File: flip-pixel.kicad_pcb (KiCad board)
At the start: 2 copper layers, 177 parts, among them Q1 DMN62D0U-7, Q10 STS8DN6LF6AG, Q11 DMN62D0U-7, Q12 DMN62D0U-7, Q13 STS8DN6LF6AG, Q14 DMN62D0U-7, Q15 DMN62D0U-7, Q16 STS8DN6LF6AG, Q17 DMN62D0U-7, Q18 DMN62D0U-7, Q19 STS8DN6LF6AG, Q2 DMN62D0U-7, Q20 DMN62D0U-7, Q21 DMN62D0U-7, Q22 STS8DN6LF6AG, Q23 DMN62D0U-7, Q24 DMN62D0U-7, Q25 STS8DN6LF6AG, Q26 DMN62D0U-7, Q27 DMN62D0U-7, Q28 STS8DN6LF6AG, Q29 DMN62D0U-7, Q3 DMN62D0U-7, Q30 DMN62D0U-7, Q31 STS8DN6LF6AG, Q4 STS8DN6LF6AG, Q5 DMN62D0U-7, Q6 DMN62D0U-7, Q7 STS8DN6LF6AG, Q8 DMN62D0U-7, Q9 DMN62D0U-7, U1 LM2665M6

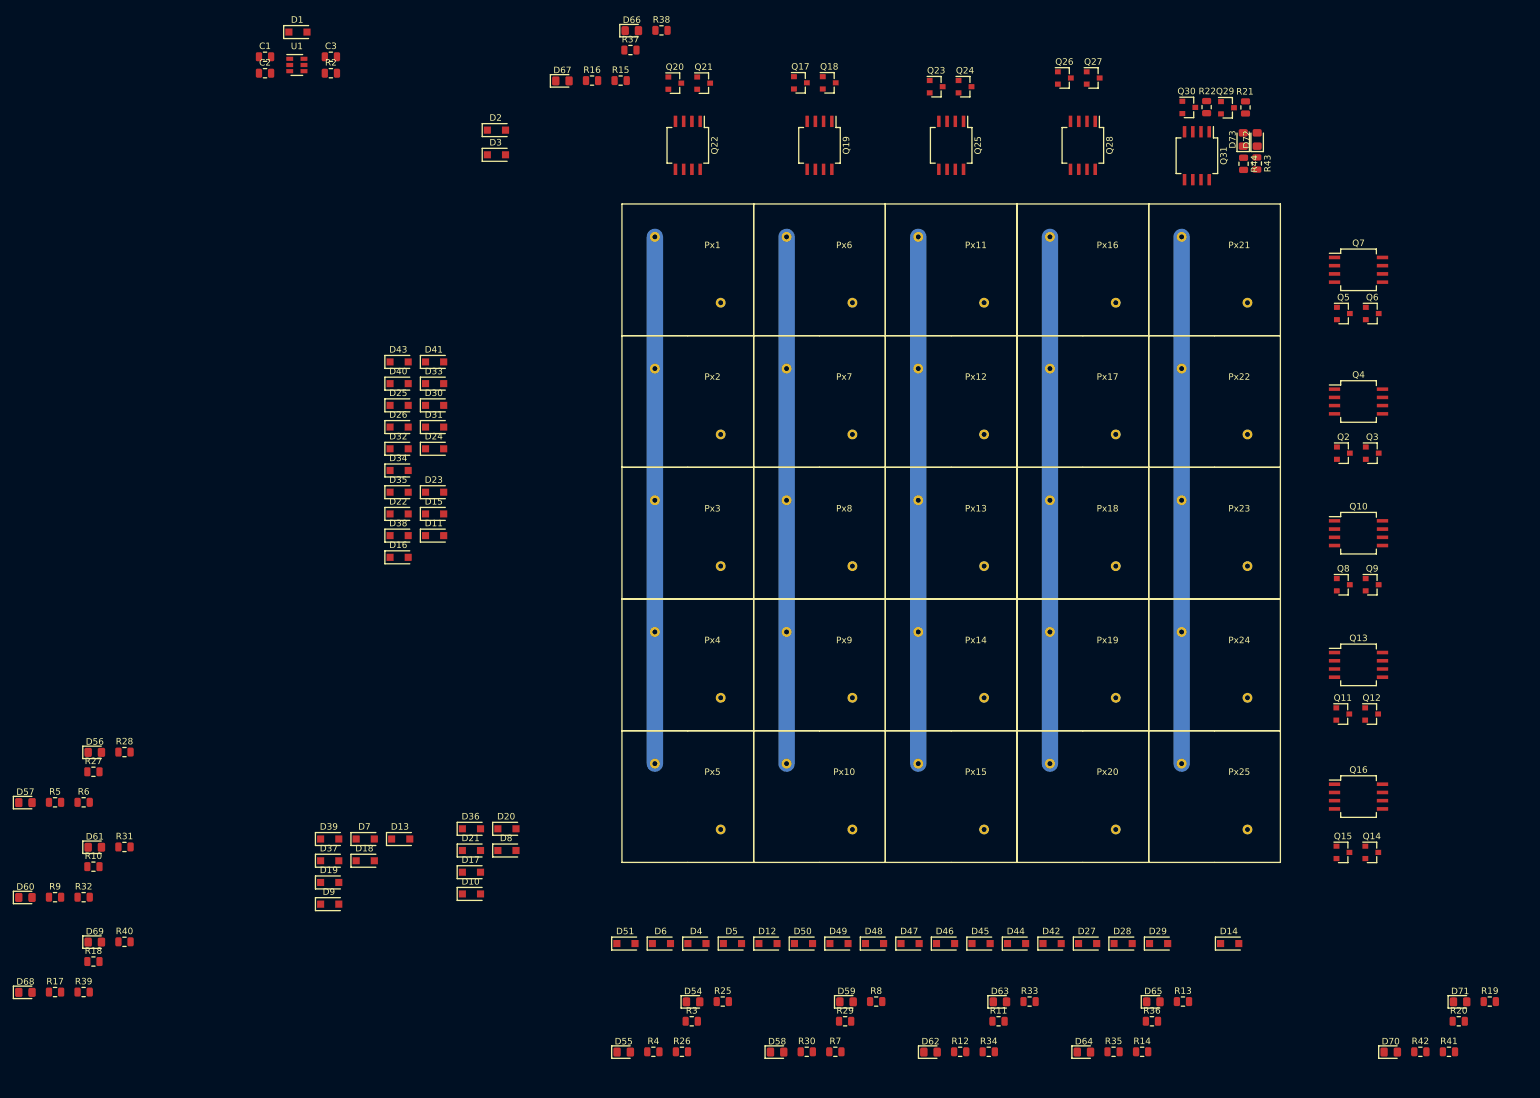
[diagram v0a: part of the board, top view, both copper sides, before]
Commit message: Pixel Matrix and started Driving Circuits
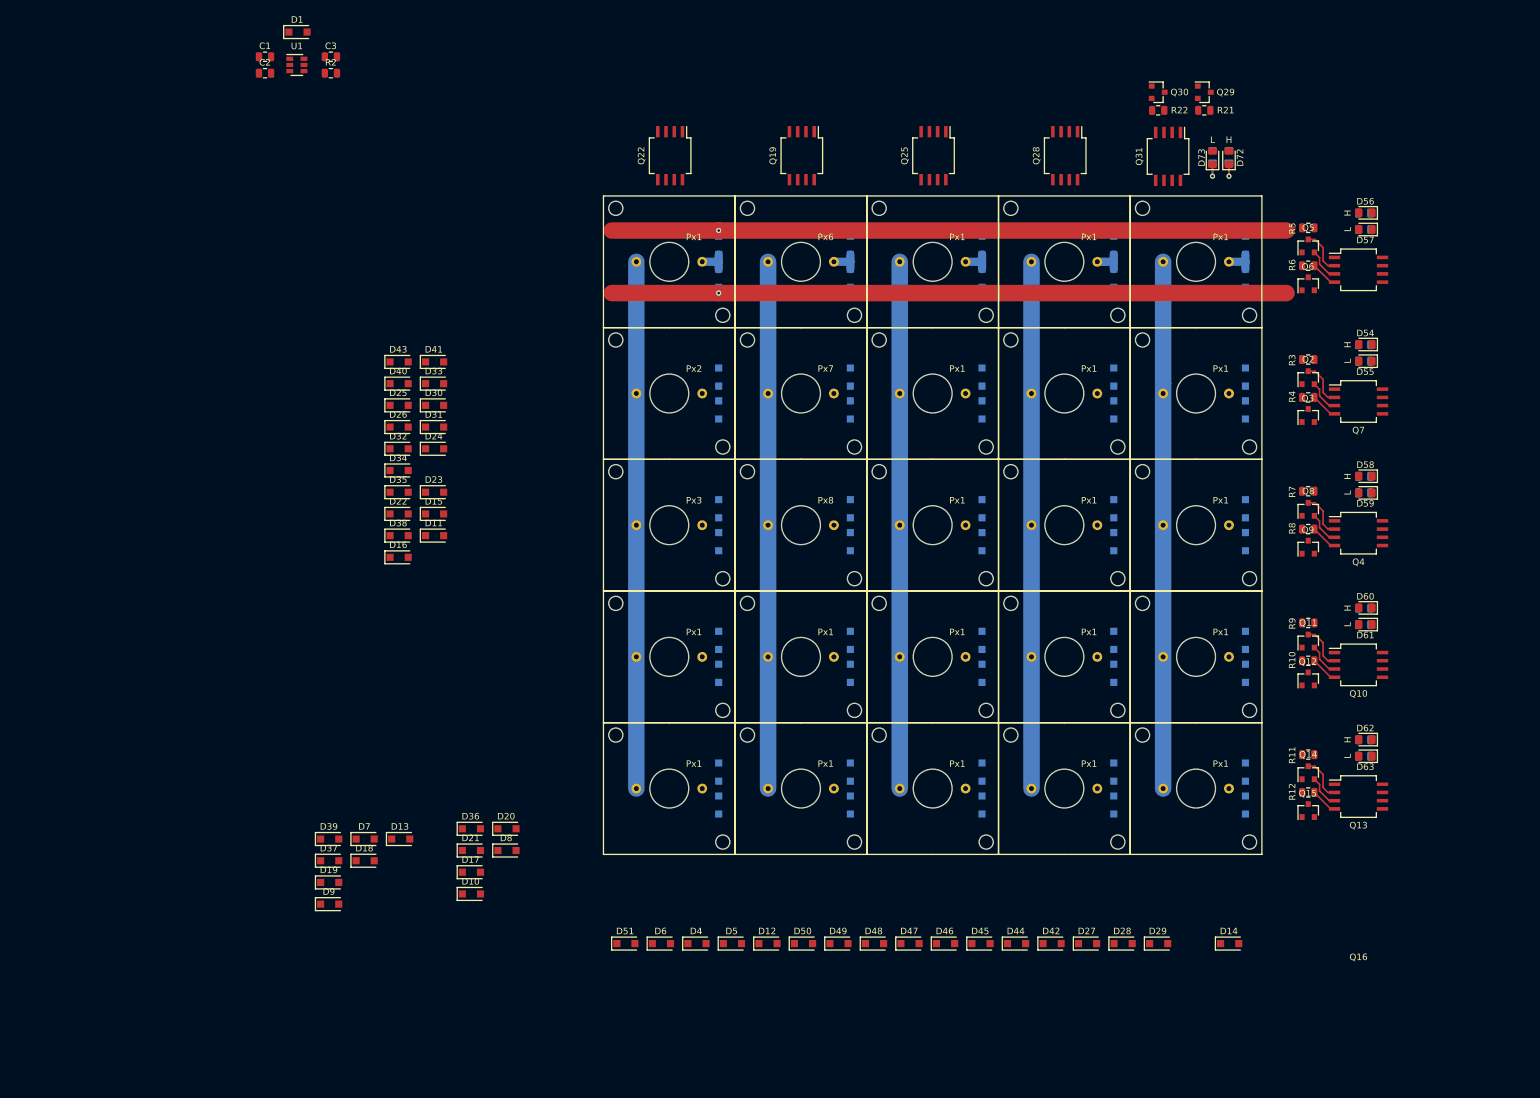
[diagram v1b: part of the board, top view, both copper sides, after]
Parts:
- removed the D2 at (141.0, 31.8)
- removed the D3 at (141.0, 35.6)
- removed D64, D65, D66, D67, D68, D69, D70, D71: LED_Green, LED_SMD:LED_0805_2012Metric_Pad1.15x1.40mm_HandSolder
- removed the Px1 at (170.5, 53.3)
- removed Px10, Px11, Px12, Px13, Px14, Px15, Px16, Px17, Px18, Px19, Px20, Px21, Px22, Px23, Px24, Px25, Px4, Px5, Px9: FlipPixel, Custom-Footprints:Flip-Pixel
- removed Q17, Q18, Q20, Q21, Q23, Q24, Q26, Q27: DMN62D0U-7, Package_TO_SOT_SMD:SOT-23
- removed R13, R14, R15, R16, R17, R18, R19, R20, R35, R36, R37, R38, R39, R40, R41, R42: R, Resistor_SMD:R_0805_2012Metric
- added D2: Diode, Diode_SMD:D_SOD-123F, B.Cu at (256.5, 130.8)
- added D2: Diode, Diode_SMD:D_SOD-123F, B.Cu at (236.2, 49.5)
- added D2: Diode, Diode_SMD:D_SOD-123F, B.Cu at (215.9, 130.8)
- added D2: Diode, Diode_SMD:D_SOD-123F, B.Cu at (215.9, 110.5)
- added D2: Diode, Diode_SMD:D_SOD-123F, B.Cu at (215.9, 90.2)
- added D2: Diode, Diode_SMD:D_SOD-123F, B.Cu at (215.9, 69.8)
- added D2: Diode, Diode_SMD:D_SOD-123F, B.Cu at (215.9, 49.5)
- added D2: Diode, Diode_SMD:D_SOD-123F, B.Cu at (195.6, 130.8)
- added D2: Diode, Diode_SMD:D_SOD-123F, B.Cu at (195.6, 110.5)
- added D2: Diode, Diode_SMD:D_SOD-123F, B.Cu at (195.6, 90.2)
- added D2: Diode, Diode_SMD:D_SOD-123F, B.Cu at (195.6, 69.8)
- added D2: Diode, Diode_SMD:D_SOD-123F, B.Cu at (256.5, 110.5)
- added D2: Diode, Diode_SMD:D_SOD-123F, B.Cu at (195.6, 49.5)
- added D2: Diode, Diode_SMD:D_SOD-123F, B.Cu at (175.3, 130.8)
- added D2: Diode, Diode_SMD:D_SOD-123F, B.Cu at (175.3, 110.5)
- added D2: Diode, Diode_SMD:D_SOD-123F, B.Cu at (175.3, 90.2)
- added D2: Diode, Diode_SMD:D_SOD-123F, B.Cu at (175.3, 69.8)
- added D2: Diode, Diode_SMD:D_SOD-123F, B.Cu at (175.3, 49.5)
- added D2: Diode, Diode_SMD:D_SOD-123F, B.Cu at (256.5, 90.2)
- added D2: Diode, Diode_SMD:D_SOD-123F, B.Cu at (256.5, 69.8)
- added D2: Diode, Diode_SMD:D_SOD-123F, B.Cu at (256.5, 49.5)
- added D2: Diode, Diode_SMD:D_SOD-123F, B.Cu at (236.2, 130.8)
- added D2: Diode, Diode_SMD:D_SOD-123F, B.Cu at (236.2, 110.5)
- added D2: Diode, Diode_SMD:D_SOD-123F, B.Cu at (236.2, 90.2)
- added D2: Diode, Diode_SMD:D_SOD-123F, B.Cu at (236.2, 69.8)
- added D3: Diode, Diode_SMD:D_SOD-123F, B.Cu at (256.5, 135.9)
- added D3: Diode, Diode_SMD:D_SOD-123F, B.Cu at (236.2, 54.6)
- added D3: Diode, Diode_SMD:D_SOD-123F, B.Cu at (215.9, 135.9)
- added D3: Diode, Diode_SMD:D_SOD-123F, B.Cu at (215.9, 115.6)
- added D3: Diode, Diode_SMD:D_SOD-123F, B.Cu at (215.9, 95.2)
- added D3: Diode, Diode_SMD:D_SOD-123F, B.Cu at (215.9, 74.9)
- added D3: Diode, Diode_SMD:D_SOD-123F, B.Cu at (215.9, 54.6)
- added D3: Diode, Diode_SMD:D_SOD-123F, B.Cu at (195.6, 135.9)
- added D3: Diode, Diode_SMD:D_SOD-123F, B.Cu at (195.6, 115.6)
- added D3: Diode, Diode_SMD:D_SOD-123F, B.Cu at (195.6, 95.2)
- added D3: Diode, Diode_SMD:D_SOD-123F, B.Cu at (195.6, 74.9)
- added D3: Diode, Diode_SMD:D_SOD-123F, B.Cu at (256.5, 115.6)
- added D3: Diode, Diode_SMD:D_SOD-123F, B.Cu at (195.6, 54.6)
- added D3: Diode, Diode_SMD:D_SOD-123F, B.Cu at (175.3, 135.9)
- added D3: Diode, Diode_SMD:D_SOD-123F, B.Cu at (175.3, 115.6)
- added D3: Diode, Diode_SMD:D_SOD-123F, B.Cu at (175.3, 95.2)
- added D3: Diode, Diode_SMD:D_SOD-123F, B.Cu at (175.3, 74.9)
- added D3: Diode, Diode_SMD:D_SOD-123F, B.Cu at (175.3, 54.6)
- added D3: Diode, Diode_SMD:D_SOD-123F, B.Cu at (256.5, 95.2)
- added D3: Diode, Diode_SMD:D_SOD-123F, B.Cu at (256.5, 74.9)
- added D3: Diode, Diode_SMD:D_SOD-123F, B.Cu at (256.5, 54.6)
- added D3: Diode, Diode_SMD:D_SOD-123F, B.Cu at (236.2, 135.9)
- added D3: Diode, Diode_SMD:D_SOD-123F, B.Cu at (236.2, 115.6)
- added D3: Diode, Diode_SMD:D_SOD-123F, B.Cu at (236.2, 95.2)
- added D3: Diode, Diode_SMD:D_SOD-123F, B.Cu at (236.2, 74.9)
- added Px1: FlipPixel, Custom-Footprints:Flip-Pixel, F.Cu at (248.9, 133.3)
- added Px1: FlipPixel, Custom-Footprints:Flip-Pixel, F.Cu at (228.6, 52.1)
- added Px1: FlipPixel, Custom-Footprints:Flip-Pixel, F.Cu at (208.3, 133.3)
- added Px1: FlipPixel, Custom-Footprints:Flip-Pixel, F.Cu at (208.3, 113.0)
- added Px1: FlipPixel, Custom-Footprints:Flip-Pixel, F.Cu at (208.3, 92.7)
- added Px1: FlipPixel, Custom-Footprints:Flip-Pixel, F.Cu at (208.3, 72.4)
- added Px1: FlipPixel, Custom-Footprints:Flip-Pixel, F.Cu at (208.3, 52.1)
- added Px1: FlipPixel, Custom-Footprints:Flip-Pixel, F.Cu at (188.0, 133.3)
- added Px1: FlipPixel, Custom-Footprints:Flip-Pixel, F.Cu at (188.0, 113.0)
- added Px1: FlipPixel, Custom-Footprints:Flip-Pixel, F.Cu at (167.6, 133.3)
- added Px1: FlipPixel, Custom-Footprints:Flip-Pixel, F.Cu at (167.6, 113.0)
- added Px1: FlipPixel, Custom-Footprints:Flip-Pixel, F.Cu at (248.9, 113.0)
- added Px1: FlipPixel, Custom-Footprints:Flip-Pixel, F.Cu at (167.6, 52.1)
- added Px1: FlipPixel, Custom-Footprints:Flip-Pixel, F.Cu at (248.9, 92.7)
- added Px1: FlipPixel, Custom-Footprints:Flip-Pixel, F.Cu at (248.9, 72.4)
- added Px1: FlipPixel, Custom-Footprints:Flip-Pixel, F.Cu at (248.9, 52.1)
- added Px1: FlipPixel, Custom-Footprints:Flip-Pixel, F.Cu at (228.6, 133.3)
- added Px1: FlipPixel, Custom-Footprints:Flip-Pixel, F.Cu at (228.6, 113.0)
- added Px1: FlipPixel, Custom-Footprints:Flip-Pixel, F.Cu at (228.6, 92.7)
- added Px1: FlipPixel, Custom-Footprints:Flip-Pixel, F.Cu at (228.6, 72.4)
- R25, R26, R27, R28, R29, R30, R31, R32, R33, R34, R43, R44: moved to B.Cu
- moved D57 224.9 mm to (275.0, 47.1), turned to 180 degrees
- moved R27 214.2 mm to (274.9, 44.5), turned to 180 degrees
- moved D56 213.0 mm to (275.0, 44.5), turned to 180 degrees
- moved R5 212.7 mm to (266.2, 46.8)
- moved D60 211.5 mm to (275.0, 105.5), turned to 180 degrees
- moved R28 207.6 mm to (274.9, 47.1), turned to 180 degrees
- moved R6 206.3 mm to (266.2, 52.7)
- moved R32 202.0 mm to (274.9, 108.0), turned to 180 degrees
- moved D61 199.0 mm to (275.0, 108.0), turned to 180 degrees
- moved R9 197.9 mm to (266.2, 107.8)
- moved R31 194.8 mm to (274.9, 105.5), turned to 180 degrees
- moved R10 190.1 mm to (266.2, 113.6)
- moved D55 156.4 mm to (275.0, 67.4), turned to 180 degrees
- moved R26 149.8 mm to (274.9, 67.4), turned to 180 degrees
- moved D54 145.1 mm to (275.0, 64.8), turned to 180 degrees
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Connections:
- Px2 pad 1: Net-(D4-Pad1) -> Net-(D2-Pad1)
- Px3 pad 1: Net-(D6-Pad1) -> Net-(D2-Pad1)
- Px6 pad 1: Net-(D12-Pad1) -> Net-(D2-Pad1)
- Px6 pad 2: /PixelMatrix/Col_2 -> /PixelMatrix/Col_1
- Px7 pad 1: Net-(D14-Pad1) -> Net-(D2-Pad1)
- Px7 pad 2: /PixelMatrix/Col_2 -> /PixelMatrix/Col_1
- Px8 pad 1: Net-(D16-Pad1) -> Net-(D2-Pad1)
- Px8 pad 2: /PixelMatrix/Col_2 -> /PixelMatrix/Col_1
- Q19 pad 1: /PixelMatrix/Col_2 -> /PixelMatrix/Col_5
- Q19 pad 2: /Column2/Gate_H -> /Column5/Gate_H
- Q19 pad 4: /Column2/Gate_L -> /Column5/Gate_L
- Q19 pad 5: /PixelMatrix/Col_2 -> /PixelMatrix/Col_5
- Q19 pad 6: /PixelMatrix/Col_2 -> /PixelMatrix/Col_5
- Q22 pad 1: /PixelMatrix/Col_1 -> /PixelMatrix/Col_5
- Q22 pad 2: /Column1/Gate_H -> /Column5/Gate_H
- Q22 pad 4: /Column1/Gate_L -> /Column5/Gate_L
- Q22 pad 5: /PixelMatrix/Col_1 -> /PixelMatrix/Col_5
- Q22 pad 6: /PixelMatrix/Col_1 -> /PixelMatrix/Col_5
- Q25 pad 1: /PixelMatrix/Col_3 -> /PixelMatrix/Col_5
- Q25 pad 2: /Column3/Gate_H -> /Column5/Gate_H
- Q25 pad 4: /Column3/Gate_L -> /Column5/Gate_L
- Q25 pad 5: /PixelMatrix/Col_3 -> /PixelMatrix/Col_5
- Q25 pad 6: /PixelMatrix/Col_3 -> /PixelMatrix/Col_5
- Q28 pad 1: /PixelMatrix/Col_4 -> /PixelMatrix/Col_5
- Q28 pad 2: /Column4/Gate_H -> /Column5/Gate_H
- Q28 pad 4: /Column4/Gate_L -> /Column5/Gate_L
- Q28 pad 5: /PixelMatrix/Col_4 -> /PixelMatrix/Col_5
- Q28 pad 6: /PixelMatrix/Col_4 -> /PixelMatrix/Col_5
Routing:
- net /PixelMatrix/Col_1: track 81.3 -> 406.4 mm
- net /Row1/Low: track 0.00 -> 105.0 mm, vias 0 -> 1
- net /Row1/High: track 0.00 -> 105.0 mm, vias 0 -> 1
- net /PixelMatrix/Col_5: track 81.3 -> 0.00 mm
- net /PixelMatrix/Col_4: track 81.3 -> 0.00 mm
- net /PixelMatrix/Col_3: track 81.3 -> 0.00 mm
- net /PixelMatrix/Col_2: track 81.3 -> 0.00 mm
- net GND: track 0.00 -> 25.4 mm
- net Net-(D2-Pad1): track 0.00 -> 24.1 mm
- net /Row5/Gate_H: track 0.00 -> 6.93 mm
- net /Row3/Gate_H: track 0.00 -> 6.93 mm
- net /Row4/Gate_H: track 0.00 -> 6.93 mm
- net /Row2/Gate_H: track 0.00 -> 6.93 mm
- net /Row1/Gate_H: track 0.00 -> 6.93 mm
- net /Row5/Gate_L: track 0.00 -> 4.17 mm
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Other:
- board text added: "H"
- board text added: "L"

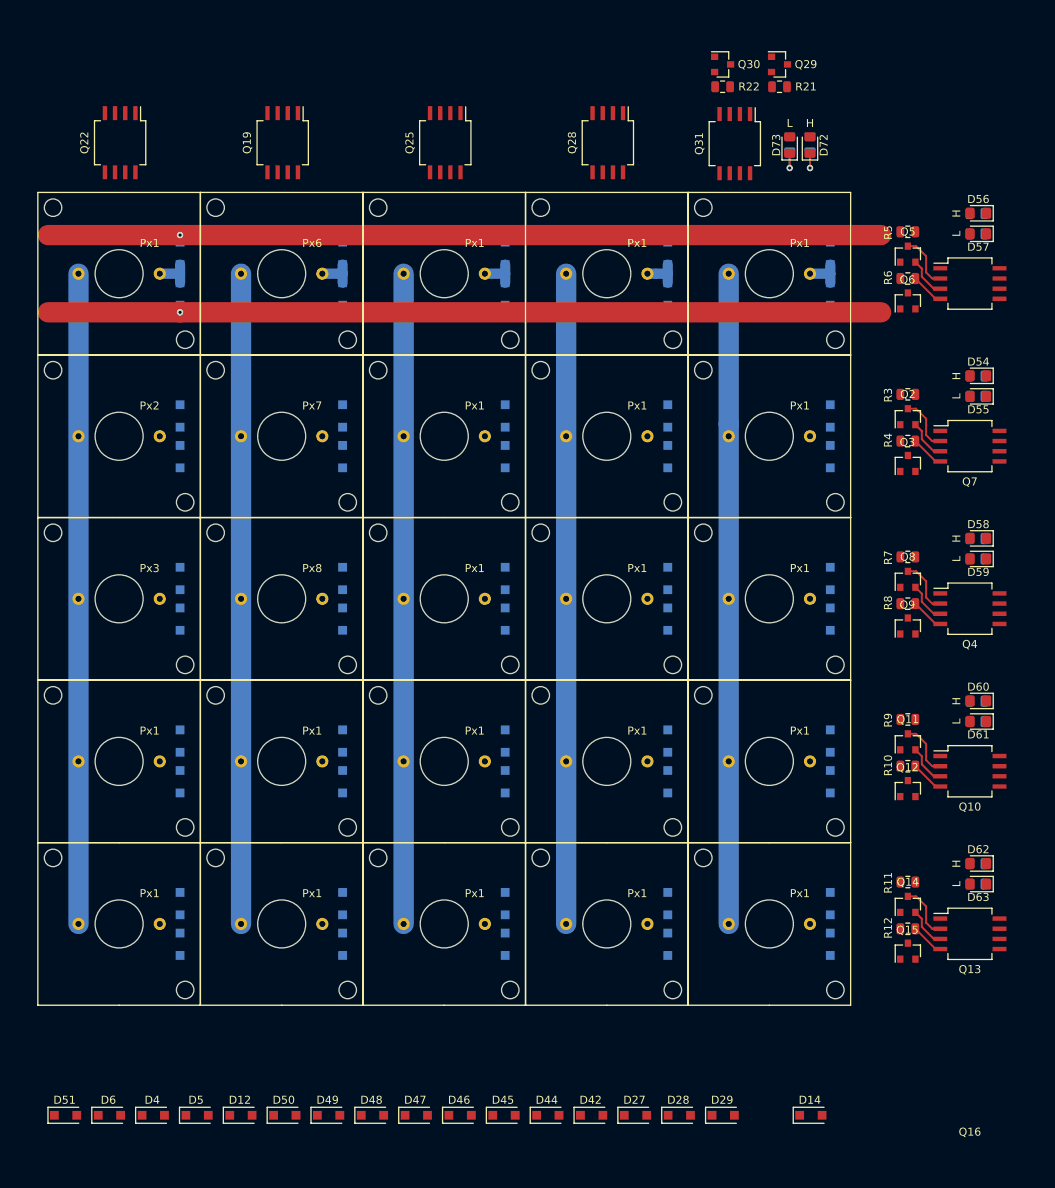
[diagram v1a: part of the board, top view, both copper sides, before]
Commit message: Layout for single driving circuit
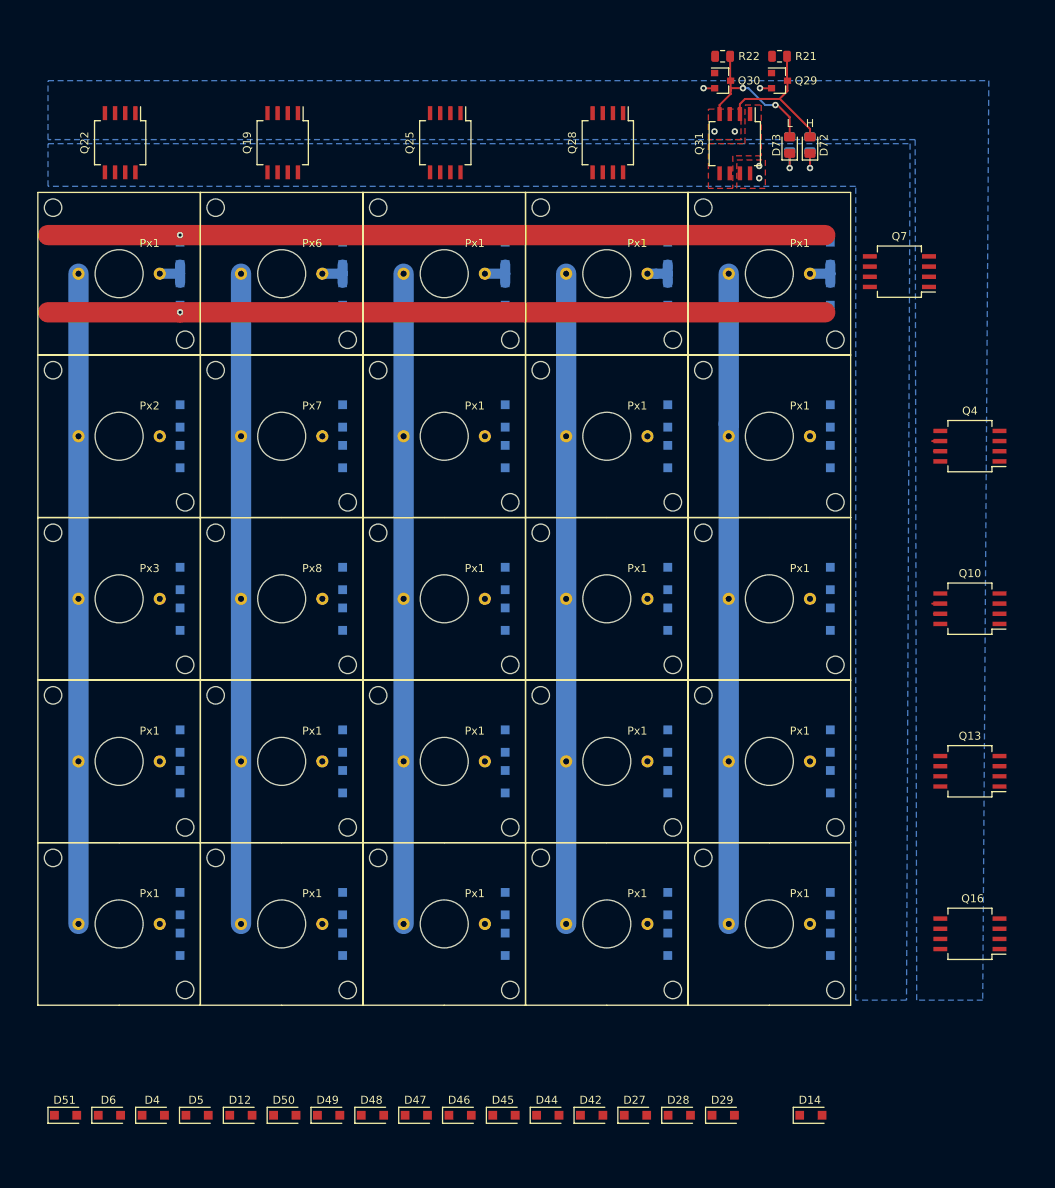
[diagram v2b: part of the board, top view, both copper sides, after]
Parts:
- removed D54, D55, D56, D57, D58, D59, D60, D61, D62, D63: LED_Green, LED_SMD:LED_0805_2012Metric_Pad1.15x1.40mm_HandSolder
- removed Q11, Q12, Q14, Q15, Q2, Q3, Q5, Q6, Q8, Q9: DMN62D0U-7, Package_TO_SOT_SMD:SOT-23
- removed R10, R11, R12, R25, R26, R27, R28, R29, R3, R30, R31, R32, R33, R34, R4, R5, R6, R7, R8, R9: R, Resistor_SMD:R_0805_2012Metric
- moved Q7 8.94 mm to (265.2, 51.8), turned to 180 degrees
- moved R21 3.81 mm to (250.2, 24.9)
- moved R22 3.81 mm to (243.1, 24.9)
- moved Q29 2.03 mm to (250.2, 27.9)
- moved Q30 2.03 mm to (243.1, 27.9)
- turned Q10 to 180 degrees
- turned Q13 to 180 degrees
- turned Q16 to 180 degrees
- turned Q4 to 180 degrees
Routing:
- net GND: track 25.4 -> 2.83 mm, vias 0 -> 4
- net /Column5/Gate_L: track 0.00 -> 19.4 mm, vias 0 -> 2
- net /Column5/Gate_H: track 0.00 -> 18.9 mm
- net /Row1/Low: track 105.0 -> 98.0 mm
- net /Row1/High: track 105.0 -> 98.0 mm
- net /Row5/Gate_H: track 6.93 -> 0.00 mm
- net /Row3/Gate_H: track 6.93 -> 0.00 mm
- net /Row4/Gate_H: track 6.93 -> 0.00 mm
- net /Row2/Gate_H: track 6.93 -> 0.00 mm
- net /Row1/Gate_H: track 6.93 -> 0.00 mm
- net /Row5/Gate_L: track 4.17 -> 0.00 mm
- net /Row4/Gate_L: track 4.17 -> 0.00 mm
- net /Row2/Gate_L: track 4.17 -> 0.00 mm
- net /Row1/Gate_L: track 4.17 -> 0.00 mm
- net /Row3/Gate_L: track 4.17 -> 0.00 mm
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- added copper zone on B.Cu, net +5V
- added copper zone on F.Cu, net +5V
- added copper zone on F.Cu, net /PixelMatrix/Col_5
- added copper zone on B.Cu, net GND
- added copper zone on F.Cu, net GND

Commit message: Fixed a footprint mistake
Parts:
- Q10, Q13, Q16, Q19, Q22, Q25, Q28, Q31, Q4, Q7: footprint Package_SO:SO-8_5.3x6.2mm_P1.27mm -> Package_SO:SO-8_3.9x4.9mm_P1.27mm
- moved Q19 3.69 mm to (184.4, 35.8)
- moved Q22 3.69 mm to (164.1, 35.8)
- moved Q25 3.69 mm to (204.7, 35.8)
- moved Q28 3.69 mm to (225.0, 35.8)
- moved D72 0.76 mm to (254.8, 36.0)
- moved D73 0.76 mm to (252.2, 36.0)
- moved Q29 0.76 mm to (251.0, 27.9)
- moved Q30 0.76 mm to (243.8, 27.9)
- moved Q31 0.76 mm to (245.4, 35.8)
- moved R21 0.76 mm to (251.0, 24.9)
- moved R22 0.76 mm to (243.8, 24.9)
- moved R43 0.76 mm to (254.8, 35.8)
- moved R44 0.76 mm to (252.2, 35.8)
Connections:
- Px2 pad 1: Net-(D2-Pad1) -> Net-(D4-Pad1)
- Px3 pad 1: Net-(D2-Pad1) -> Net-(D6-Pad1)
- Px6 pad 1: Net-(D2-Pad1) -> Net-(D12-Pad1)
- Px6 pad 2: /PixelMatrix/Col_1 -> /PixelMatrix/Col_2
- Px7 pad 1: Net-(D2-Pad1) -> Net-(D14-Pad1)
- Px7 pad 2: /PixelMatrix/Col_1 -> /PixelMatrix/Col_2
- Px8 pad 1: Net-(D2-Pad1) -> Net-(D16-Pad1)
- Px8 pad 2: /PixelMatrix/Col_1 -> /PixelMatrix/Col_2
- Q19 pad 1: /PixelMatrix/Col_5 -> /PixelMatrix/Col_2
- Q19 pad 2: /Column5/Gate_H -> /Column2/Gate_H
- Q19 pad 4: /Column5/Gate_L -> /Column2/Gate_L
- Q19 pad 5: /PixelMatrix/Col_5 -> /PixelMatrix/Col_2
- Q19 pad 6: /PixelMatrix/Col_5 -> /PixelMatrix/Col_2
- Q22 pad 1: /PixelMatrix/Col_5 -> /PixelMatrix/Col_1
- Q22 pad 2: /Column5/Gate_H -> /Column1/Gate_H
- Q22 pad 4: /Column5/Gate_L -> /Column1/Gate_L
- Q22 pad 5: /PixelMatrix/Col_5 -> /PixelMatrix/Col_1
- Q22 pad 6: /PixelMatrix/Col_5 -> /PixelMatrix/Col_1
- Q25 pad 1: /PixelMatrix/Col_5 -> /PixelMatrix/Col_3
- Q25 pad 2: /Column5/Gate_H -> /Column3/Gate_H
- Q25 pad 4: /Column5/Gate_L -> /Column3/Gate_L
- Q25 pad 5: /PixelMatrix/Col_5 -> /PixelMatrix/Col_3
- Q25 pad 6: /PixelMatrix/Col_5 -> /PixelMatrix/Col_3
- Q28 pad 1: /PixelMatrix/Col_5 -> /PixelMatrix/Col_4
- Q28 pad 2: /Column5/Gate_H -> /Column4/Gate_H
- Q28 pad 4: /Column5/Gate_L -> /Column4/Gate_L
- Q28 pad 5: /PixelMatrix/Col_5 -> /PixelMatrix/Col_4
- Q28 pad 6: /PixelMatrix/Col_5 -> /PixelMatrix/Col_4
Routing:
- net /Column5/Gate_H: track 18.9 -> 19.9 mm
- net /Column5/Gate_L: track 19.4 -> 20.1 mm
- net GND: vias 4 -> 5
